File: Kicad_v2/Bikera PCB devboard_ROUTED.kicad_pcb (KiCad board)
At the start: 4 copper layers, 60 x 40 mm, 114 parts, among them IC1 DRV5032DULPGM, IC2 BQ25630YBGR, IC3 DRV5032DULPGM, IC4 FM24V01A-G, J1 USB4105-GF-A-060, J3 ST-LINK BTB, J7 Waveshare_ePaper_module, SW1 SW_Reset, SW2 SW_Boot, U1 RT6158HWSC, U2 TCR3UG33A_LF, U3 STM32L431CCTx, U4 TPS61253F, U5 ATECC608B-SSHDA-T, U6 LC76GPAMD, U7 USBLC6-2SC6, U8 SMF05CT1G, U9 RAK11720

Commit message: PCB routing claude (deel 1)
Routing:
- net GPS_RESET: track 0.00 -> 119.4 mm, vias 0 -> 14
- net +5V: track 0.00 -> 98.9 mm, vias 0 -> 4
- net +3V3_GPS: track 0.00 -> 78.7 mm, vias 0 -> 5
- net EPAPER_RST: track 0.00 -> 72.4 mm, vias 0 -> 4
- net EPAPER_DC: track 0.00 -> 66.1 mm, vias 0 -> 4
- net I2C_SDA: track 0.00 -> 59.0 mm, vias 0 -> 8
- net EPAPER_CS: track 0.00 -> 55.0 mm, vias 0 -> 2
- net LORA_BOOT: track 0.00 -> 53.6 mm, vias 0 -> 1
- net +SYS: track 0.00 -> 50.1 mm, vias 0 -> 2
- net /MCU - Sensors - Actuators/SERVO_RSENSE: track 0.00 -> 49.0 mm, vias 0 -> 6
- net /MCU - Sensors - Actuators/DEBUG_RX: track 0.00 -> 45.8 mm, vias 0 -> 5
- net /MCU - Sensors - Actuators/SERVO_PWM: track 0.00 -> 41.9 mm, vias 0 -> 1
- net +BATT: track 0.00 -> 39.3 mm
- net +3V3: track 0.00 -> 36.9 mm, vias 0 -> 30
- net /MCU - Sensors - Actuators/ACCEL_INT2: track 0.00 -> 35.2 mm, vias 0 -> 2
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
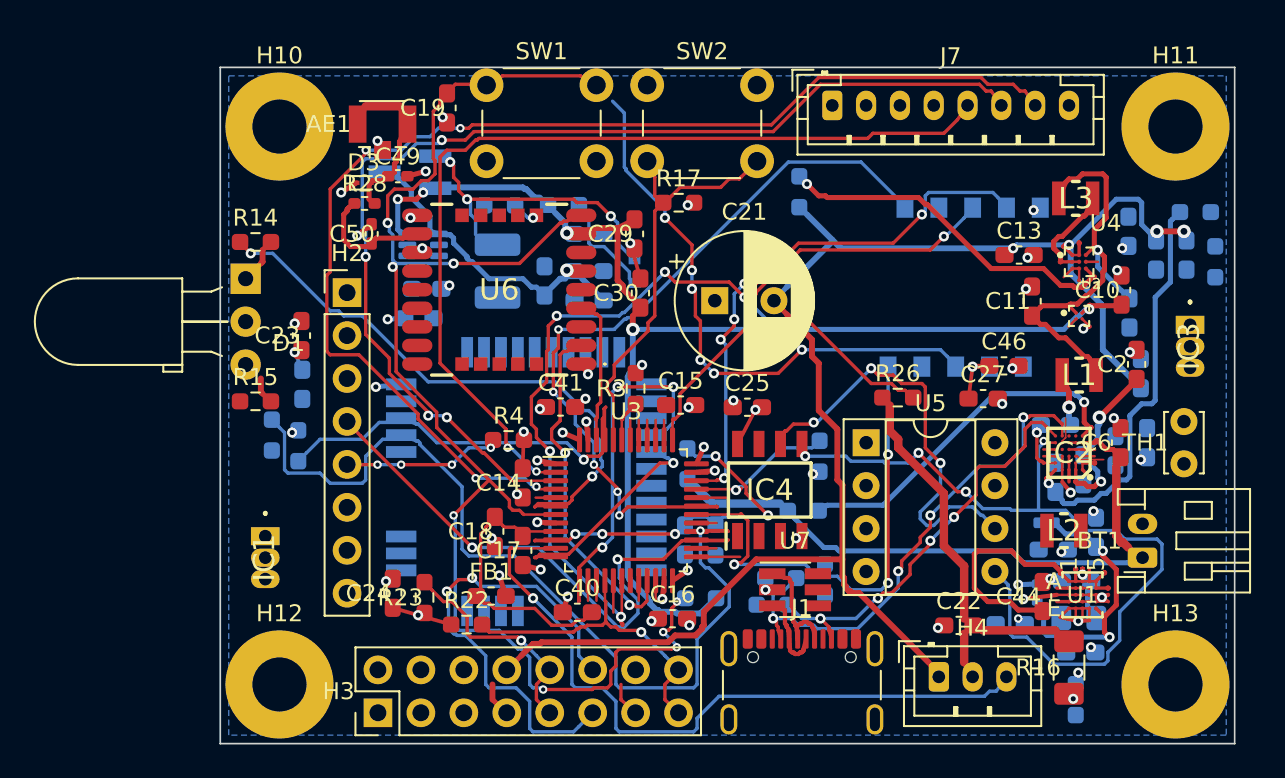
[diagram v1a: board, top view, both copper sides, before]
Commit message: PCB routing claude (deel 2)
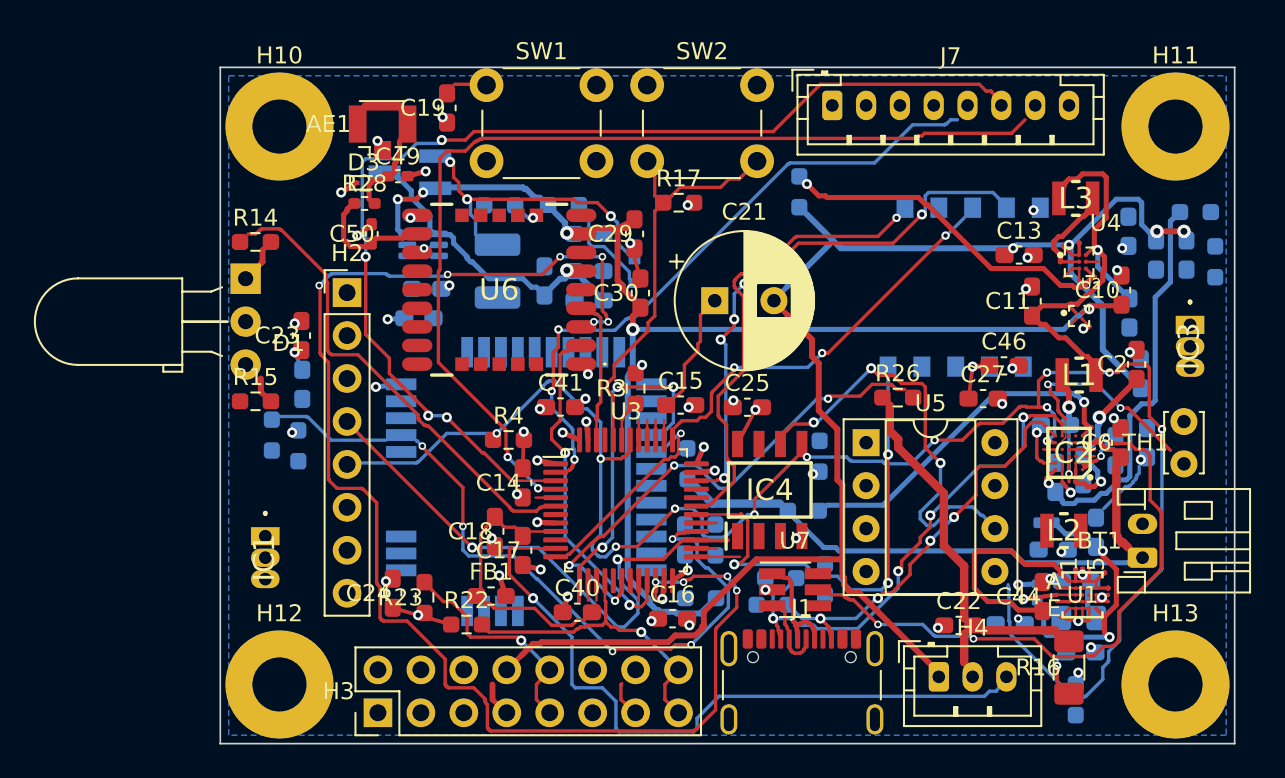
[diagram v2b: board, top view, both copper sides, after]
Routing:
- net GPS_RESET: track 119.4 -> 0.90 mm, vias 14 -> 0
- net GPS_RX: track 1.19 -> 83.7 mm, vias 0 -> 10
- net I2C_SDA: track 59.0 -> 102.2 mm, vias 8 -> 12
- net +VBUS: track 1.88 -> 36.8 mm, vias 0 -> 4
- net SPI1_MOSI: track 29.7 -> 0.00 mm, vias 2 -> 0
- net LORA_RESET: track 24.8 -> 0.00 mm, vias 1 -> 0
- net VBAT_SENSE: track 22.7 -> 0.00 mm, vias 5 -> 0
- net /MCU - Sensors - Actuators/DEBUG_RX: track 45.8 -> 26.3 mm, vias 5 -> 1
- net /MCU - Sensors - Actuators/SERVO_RSENSE: track 49.0 -> 29.7 mm, vias 6 -> 4
- net EPAPER_CS: track 55.0 -> 38.1 mm, vias 2 -> 3
- net EPAPER_RST: track 72.4 -> 57.9 mm, vias 4 -> 2
- net LORA_BOOT: track 53.6 -> 40.8 mm, vias 1 -> 5
- net Net-(IC2-TS): track 1.53 -> 12.9 mm, vias 0 -> 2
- net CHRG_INT: track 9.87 -> 0.00 mm, vias 1 -> 0
- net /MCU - Sensors - Actuators/RED LED: track 34.8 -> 27.4 mm, vias 2 -> 0
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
